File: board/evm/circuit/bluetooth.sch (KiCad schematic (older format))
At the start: 1 part

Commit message: add lots of ICs
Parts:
- removed U?: STM32F405VGTx, LQFP100, symbol STM32F405VGTx
- added U?: DA14580-QFN40, symbol DA14580-QFN40
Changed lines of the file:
@@
 EELAYER 25 0
 EELAYER END
-$Descr A2 23386 16535
+$Descr A4 11693 8268
 encoding utf-8
-Sheet 2 8
+Sheet 6 8
 Title ""
 Date ""
@@
 $EndDescr
 $Comp
-L STM32F405VGTx U?
-U 1 1 5753F449
-P 9650 6400
-F 0 "U?" H 5350 9225 50  0000 L BNN
-F 1 "STM32F405VGTx" H 13950 9225 50  0000 R BNN
-F 2 "LQFP100" H 13950 9175 50  0000 R TNN
-F 3 "" H 9650 6400 50  0000 C CNN
-	1    9650 6400
+L DA14580-QFN40 U?
+U 1 1 575491AD
+P 4450 2950
+F 0 "U?" H 4350 3000 60  0000 C CNN
+F 1 "DA14580-QFN40" H 4400 2850 60  0000 C CNN
+F 2 "" H 4350 3000 60  0000 C CNN
+F 3 "" H 4350 3000 60  0000 C CNN
+	1    4450 2950
 	1    0    0    -1
 $EndComp

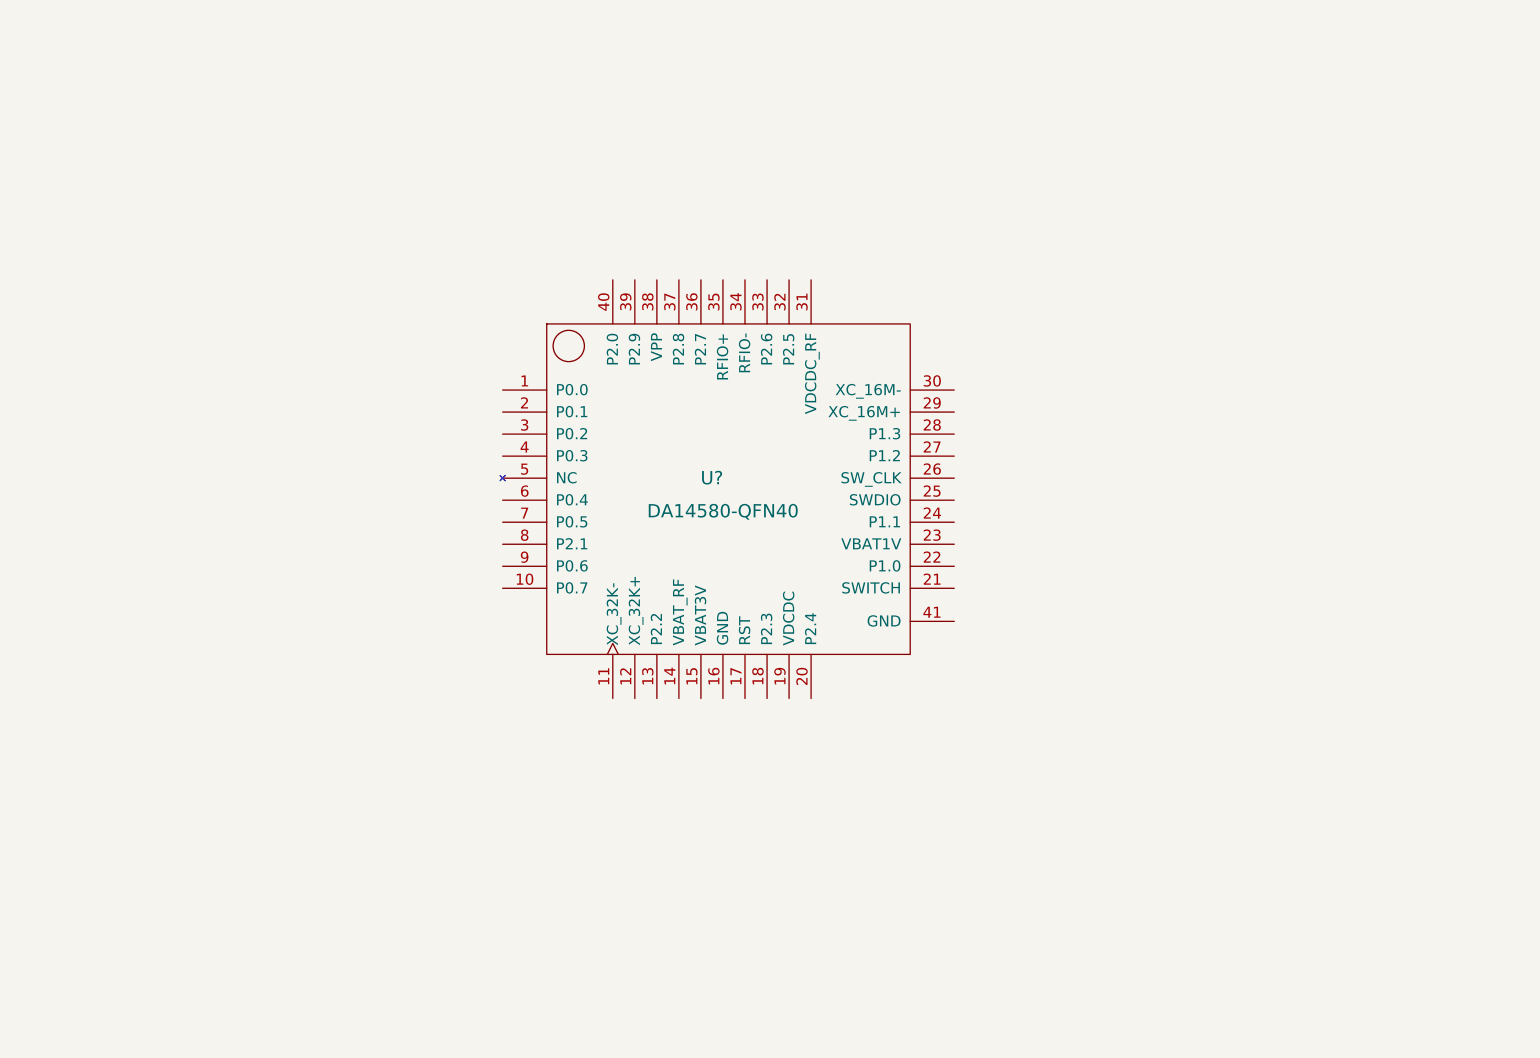
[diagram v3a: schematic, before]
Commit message: still working for sch
All done except for battery, which need more consideration on scheme of
QC2.0 (or QC3.0?), bidirectional charge.
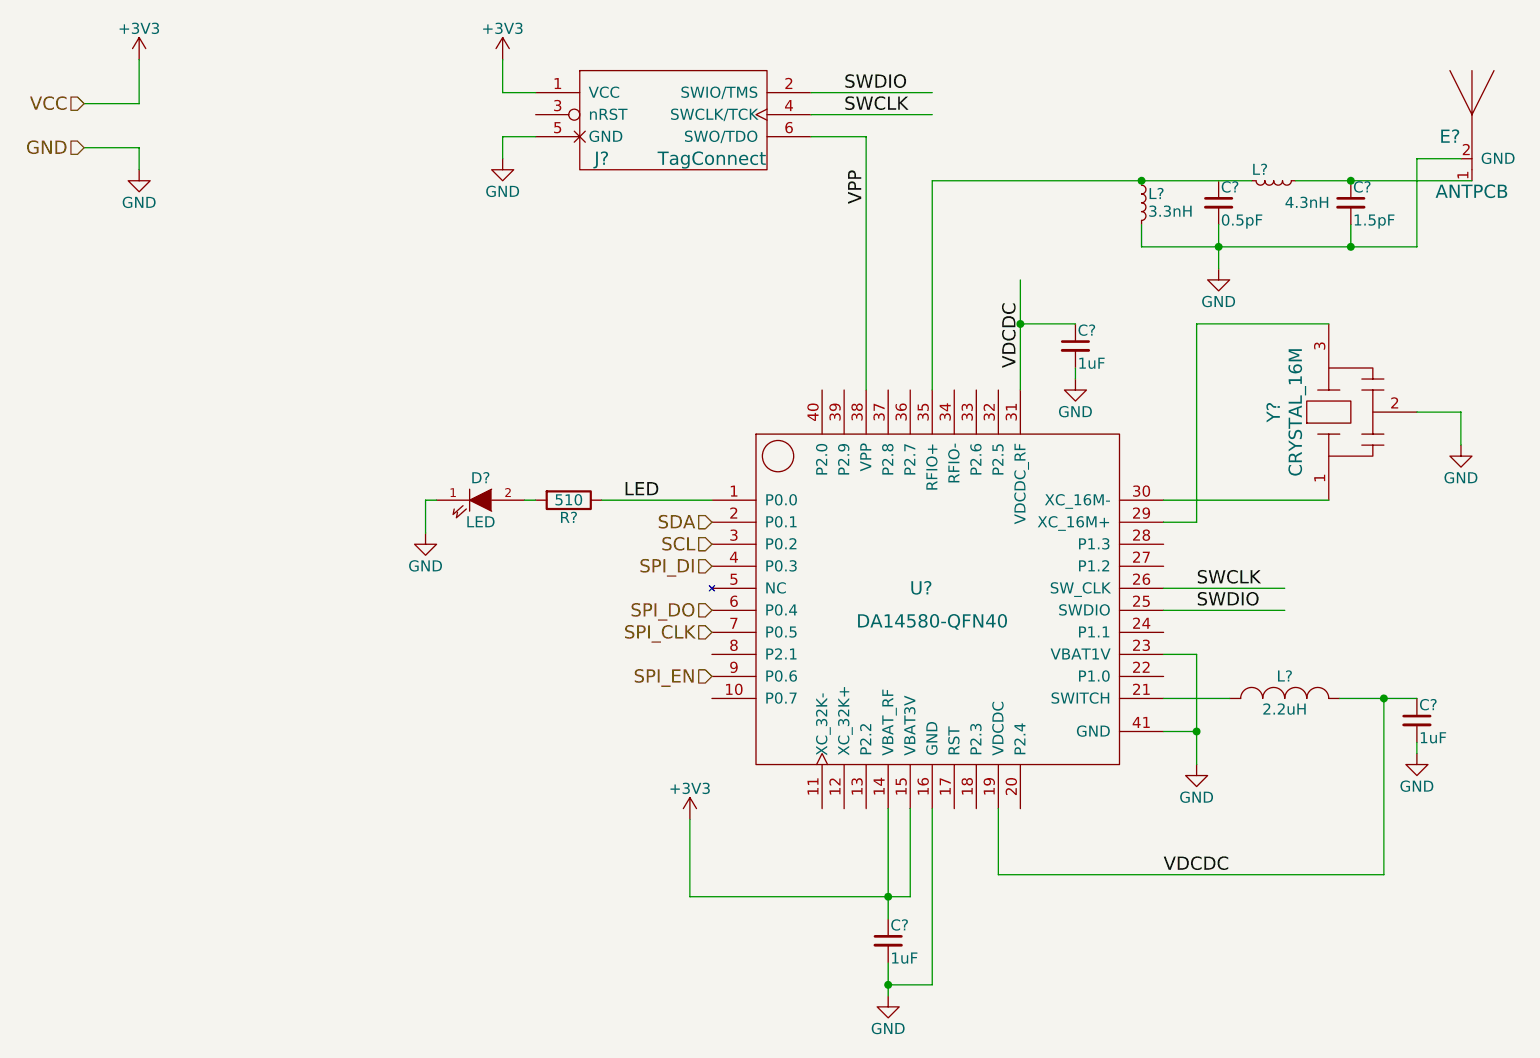
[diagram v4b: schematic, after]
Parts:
- added C? (x3): 1uF, symbol C_Small
- added C?: 0.5pF, symbol C_Small
- added C?: 1.5pF, symbol C_Small
- added D?: LED, symbol LED
- added E?: ANTPCB, symbol ANTPCB
- added J?: TagConnect, symbol TagConnect
- added L?: 2.2uH, symbol INDUCTOR_SMALL
- added L?: 3.3nH, symbol L_Small
- added L?: 4.3nH, symbol L_Small
- added R?: 510, symbol R
- added Y?: CRYSTAL_16M, symbol CRYSTAL_SMT
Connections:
- net labels added: +3V3, GND, LED, SCL, SDA, SPI_CLK, SPI_DI, SPI_DO, SPI_EN, SWCLK, SWDIO, VCC, VDCDC, VPP
- wire segments 0 -> 63
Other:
- moved on the sheet: U?

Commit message: working on qc3
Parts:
- gave numbers to parts that had none: 14
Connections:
- wire segments 63 -> 52
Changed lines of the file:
@@
 LIBS:contrib
 LIBS:valves
+LIBS:stm8
+LIBS:stm32
+LIBS:74xgxx
+LIBS:ac-dc
+LIBS:actel
 LIBS:Altera
-LIBS:my_kicad
+LIBS:analog_devices
+LIBS:battery_management
+LIBS:bbd
+LIBS:brooktre
+LIBS:cmos_ieee
+LIBS:dc-dc
+LIBS:diode
+LIBS:elec-unifil
+LIBS:ESD_Protection
+LIBS:ftdi
+LIBS:gennum
+LIBS:graphic
+LIBS:hc11
+LIBS:ir
+LIBS:Lattice
+LIBS:logo
+LIBS:maxim
+LIBS:microchip_dspic33dsc
+LIBS:microchip_pic10mcu
+LIBS:microchip_pic12mcu
+LIBS:microchip_pic16mcu
+LIBS:microchip_pic18mcu
+LIBS:microchip_pic32mcu
+LIBS:motor_drivers
+LIBS:msp430
+LIBS:nordicsemi
+LIBS:nxp_armmcu
+LIBS:onsemi
 LIBS:Oscillators
+LIBS:powerint
+LIBS:Power_Management
+LIBS:pspice
+LIBS:references
+LIBS:relays
+LIBS:rfcom
+LIBS:sensors
+LIBS:silabs
+LIBS:supertex
+LIBS:switches
+LIBS:transf
+LIBS:ttl_ieee
+LIBS:video
+LIBS:Worldsemi
+LIBS:Xicor
+LIBS:Zilog
 LIBS:oh-my-keyboard-cache
 EELAYER 25 0
@@
 $EndDescr
 $Comp
-L DA14580-QFN40 U?
+L DA14580-QFN40 U7
 U 1 1 575491AD
 P 5400 3450
-F 0 "U?" H 5300 3500 60  0000 C CNN
+F 0 "U7" H 5300 3500 60  0000 C CNN
 F 1 "DA14580-QFN40" H 5350 3350 60  0000 C CNN
 F 2 "" H 5300 3500 60  0000 C CNN
@@
 SCL
 $Comp
-L +3V3 #PWR?
+L +3V3 #PWR062
 U 1 1 57594899
 P 1750 1000
-F 0 "#PWR?" H 1750 850 50  0001 C CNN
+F 0 "#PWR062" H 1750 850 50  0001 C CNN
 F 1 "+3V3" H 1750 1140 50  0000 C CNN
 F 2 "" H 1750 1000 50  0000 C CNN
@@
 	1750 1200 1750 1000
 $Comp
-L GND #PWR?
+L GND #PWR063
 U 1 1 575948B2
 P 1750 1500
-F 0 "#PWR?" H 1750 1250 50  0001 C CNN
+F 0 "#PWR063" H 1750 1250 50  0001 C CNN
 F 1 "GND" H 1750 1350 50  0000 C CNN
 F 2 "" H 1750 1500 50  0000 C CNN
@@
 	1750 1400 1750 1500
 $Comp
-L +3V3 #PWR?
+L +3V3 #PWR064
 U 1 1 575948CE
 P 4250 4450
-F 0 "#PWR?" H 4250 4300 50  0001 C CNN
+F 0 "#PWR064" H 4250 4300 50  0001 C CNN
 F 1 "+3V3" H 4250 4590 50  0000 C CNN
 F 2 "" H 4250 4450 50  0000 C CNN
@@
 	4250 4450 4250 4800
 Wire Wire Line
-	4250 4800 5150 4800
-Wire Wire Line
-	5150 4800 5250 4800
-Wire Wire Line
-	5150 4400 5150 4800
-Wire Wire Line
-	5150 4800 5150 4900
+	4250 4800 5250 4800
+Wire Wire Line
+	5150 4400 5150 4900
 Wire Wire Line
 	5250 4800 5250 4400
 Connection ~ 5150 4800
 $Comp
-L C_Small C?
+L C_Small C10
 U 1 1 57594902
 P 5150 5000
-F 0 "C?" H 5160 5070 50  0000 L CNN
+F 0 "C10" H 5160 5070 50  0000 L CNN
 F 1 "1uF" H 5160 4920 50  0000 L CNN
 F 2 "" H 5150 5000 50  0000 C CNN
@@
 $EndComp
 $Comp
-L GND #PWR?
+L GND #PWR065
 U 1 1 57594985
 P 5150 5250
-F 0 "#PWR?" H 5150 5000 50  0001 C CNN
+F 0 "#PWR065" H 5150 5000 50  0001 C CNN
 F 1 "GND" H 5150 5100 50  0000 C CNN
 F 2 "" H 5150 5250 50  0000 C CNN
@@
 $EndComp
 Wire Wire Line
-	5150 5100 5150 5200
-Wire Wire Line
-	5150 5200 5150 5250
+	5150 5100 5150 5250
 Wire Wire Line
 	5350 4400 5350 5200
@@
 Connection ~ 5150 5200
 $Comp
-L GND #PWR?
+L GND #PWR066
 U 1 1 575949DB
 P 6550 4200
-F 0 "#PWR?" H 6550 3950 50  0001 C CNN
+F 0 "#PWR066" H 6550 3950 50  0001 C CNN
 F 1 "GND" H 6550 4050 50  0000 C CNN
 F 2 "" H 6550 4200 50  0000 C CNN
@@
 	6400 4050 6550 4050
 Wire Wire Line
-	6550 3700 6550 4050
-Wire Wire Line
-	6550 4050 6550 4200
-$Comp
-L INDUCTOR_SMALL L?
+	6550 3700 6550 4200
+$Comp
+L INDUCTOR_SMALL L6
 U 1 1 57594A20
 P 6950 3900
-F 0 "L?" H 6950 4000 50  0000 C CNN
+F 0 "L6" H 6950 4000 50  0000 C CNN
 F 1 "2.2uH" H 6950 3850 50  0000 C CNN
 F 2 "" H 6950 3900 50  0000 C CNN
@@
 	6400 3900 6700 3900
 Wire Wire Line
-	7200 3900 7400 3900
-Wire Wire Line
-	7400 3900 7550 3900
+	7200 3900 7550 3900
 Wire Wire Line
 	7400 3900 7400 4700
@@
 VDCDC
 Wire Wire Line
-	5750 2000 5750 2200
-Wire Wire Line
-	5750 2200 5750 2500
+	5750 2000 5750 2500
 Text Label 5750 2400 1    60   ~ 0
 VDCDC
 $Comp
-L C_Small C?
+L C_Small C11
 U 1 1 57594AAC
 P 6000 2300
-F 0 "C?" H 6010 2370 50  0000 L CNN
+F 0 "C11" H 6010 2370 50  0000 L CNN
 F 1 "1uF" H 6010 2220 50  0000 L CNN
 F 2 "" H 6000 2300 50  0000 C CNN
@@
 Connection ~ 5750 2200
 $Comp
-L GND #PWR?
+L GND #PWR067
 U 1 1 57594B38
 P 6000 2450
-F 0 "#PWR?" H 6000 2200 50  0001 C CNN
+F 0 "#PWR067" H 6000 2200 50  0001 C CNN
 F 1 "GND" H 6000 2300 50  0000 C CNN
 F 2 "" H 6000 2450 50  0000 C CNN
@@
 Connection ~ 6550 4050
 $Comp
-L CRYSTAL_SMT Y?
+L CRYSTAL_SMT Y2
 U 1 1 57594EC4
 P 7200 2600
-F 0 "Y?" H 7200 2900 60  0000 C CNN
+F 0 "Y2" H 7200 2900 60  0000 C CNN
 F 1 "CRYSTAL_16M" H 7200 2800 60  0000 C CNN
 F 2 "" H 7200 2600 60  0000 C CNN
@@
 	6550 3100 6400 3100
 $Comp
-L GND #PWR?
+L GND #PWR068
 U 1 1 57594FC8
 P 7750 2750
-F 0 "#PWR?" H 7750 2500 50  0001 C CNN
+F 0 "#PWR068" H 7750 2500 50  0001 C CNN
 F 1 "GND" H 7750 2600 50  0000 C CNN
 F 2 "" H 7750 2750 50  0000 C CNN
@@
 	7750 2600 7750 2750
 $Comp
-L TagConnect J?
+L TagConnect J2
 U 1 1 57595027
 P 4150 1300
-F 0 "J?" H 3850 1150 60  0000 C CNN
+F 0 "J2" H 3850 1150 60  0000 C CNN
 F 1 "TagConnect" H 4350 1150 60  0000 C CNN
 F 2 "" H 4000 1350 60  0000 C CNN
@@
 $EndComp
 $Comp
-L +3V3 #PWR?
+L +3V3 #PWR069
 U 1 1 5759512A
 P 3400 1000
-F 0 "#PWR?" H 3400 850 50  0001 C CNN
+F 0 "#PWR069" H 3400 850 50  0001 C CNN
 F 1 "+3V3" H 3400 1140 50  0000 C CNN
 F 2 "" H 3400 1000 50  0000 C CNN
@@
 	3400 1150 3550 1150
 $Comp
-L GND #PWR?
+L GND #PWR070
 U 1 1 5759517F
 P 3400 1450
-F 0 "#PWR?" H 3400 1200 50  0001 C CNN
+F 0 "#PWR070" H 3400 1200 50  0001 C CNN
 F 1 "GND" H 3400 1300 50  0000 C CNN
 F 2 "" H 3400 1450 50  0000 C CNN
@@
 SWCLK
 $Comp
-L C_Small C?
+L C_Small C14
 U 1 1 575956A9
 P 7550 4000
-F 0 "C?" H 7560 4070 50  0000 L CNN
+F 0 "C14" H 7560 4070 50  0000 L CNN
 F 1 "1uF" H 7560 3920 50  0000 L CNN
 F 2 "" H 7550 4000 50  0000 C CNN
@@
 $EndComp
 $Comp
-L GND #PWR?
+L GND #PWR071
 U 1 1 57595724
 P 7550 4150
-F 0 "#PWR?" H 7550 3900 50  0001 C CNN
+F 0 "#PWR071" H 7550 3900 50  0001 C CNN
 F 1 "GND" H 7550 4000 50  0000 C CNN
 F 2 "" H 7550 4150 50  0000 C CNN
@@
 Connection ~ 7400 3900
 $Comp
-L L_Small L?
+L L_Small L4
 U 1 1 57595AEB
 P 6300 1650
-F 0 "L?" H 6330 1690 50  0000 L CNN
+F 0 "L4" H 6330 1690 50  0000 L CNN
 F 1 "3.3nH" H 6330 1610 50  0000 L CNN
 F 2 "" H 6300 1650 50  0000 C CNN
@@
 $EndComp
 $Comp
-L L_Small L?
+L L_Small L5
 U 1 1 57595B48
 P 6900 1550
-F 0 "L?" V 6850 1450 50  0000 L CNN
+F 0 "L5" V 6850 1450 50  0000 L CNN
 F 1 "4.3nH" V 7000 1600 50  0000 L CNN
 F 2 "" H 6900 1550 50  0000 C CNN
@@
 	5350 2500 5350 1550
 Wire Wire Line
-	5350 1550 6300 1550
-Wire Wire Line
-	6300 1550 6800 1550
+	5350 1550 6800 1550
 Connection ~ 6300 1550
 $Comp
-L C_Small C?
+L C_Small C12
 U 1 1 57595F02
 P 6650 1650
-F 0 "C?" H 6660 1720 50  0000 L CNN
+F 0 "C12" H 6660 1720 50  0000 L CNN
 F 1 "0.5pF" H 6660 1570 50  0000 L CNN
 F 2 "" H 6650 1650 50  0000 C CNN
@@
 	6300 1750 6300 1850
 Wire Wire Line
-	6300 1850 6650 1850
-Wire Wire Line
-	6650 1850 7250 1850
-Wire Wire Line
-	7250 1850 7550 1850
-Wire Wire Line
-	6650 1750 6650 1850
-Wire Wire Line
-	6650 1850 6650 1950
-$Comp
-L GND #PWR?
+	6300 1850 7550 1850
+Wire Wire Line
+	6650 1750 6650 1950
+$Comp
+L GND #PWR072
 U 1 1 57595FB6
 P 6650 1950
-F 0 "#PWR?" H 6650 1700 50  0001 C CNN
+F 0 "#PWR072" H 6650 1700 50  0001 C CNN
 F 1 "GND" H 6650 1800 50  0000 C CNN
 F 2 "" H 6650 1950 50  0000 C CNN
@@
 $EndComp
 $Comp
-L C_Small C?
+L C_Small C13
 U 1 1 57596029
 P 7250 1650
-F 0 "C?" H 7260 1720 50  0000 L CNN
+F 0 "C13" H 7260 1720 50  0000 L CNN
 F 1 "1.5pF" H 7260 1570 50  0000 L CNN
 F 2 "" H 7250 1650 50  0000 C CNN
@@
 $EndComp
 Wire Wire Line
-	7000 1550 7250 1550
-Wire Wire Line
-	7250 1550 7800 1550
+	7000 1550 7800 1550
 Wire Wire Line
 	7250 1850 7250 1750
 Connection ~ 6650 1850
 $Comp
-L ANTPCB E?
+L ANTPCB E2
 U 1 1 57596217
 P 7800 1500
-F 0 "E?" H 7700 1650 60  0000 C CNN
+F 0 "E2" H 7700 1650 60  0000 C CNN
 F 1 "ANTPCB" H 7800 1400 60  0000 C CNN
 F 2 "" H 7800 1500 60  0000 C CNN
@@
 Connection ~ 7250 1850
 $Comp
-L LED D?
+L LED D9
 U 1 1 57596385
 P 3300 3000
-F 0 "D?" H 3300 3100 50  0000 C CNN
+F 0 "D9" H 3300 3100 50  0000 C CNN
 F 1 "LED" H 3300 2900 50  0000 C CNN
 F 2 "" H 3300 3000 50  0000 C CNN
@@
 	3850 3000 4350 3000
 $Comp
-L R R?
+L R R7
 U 1 1 5759657F
 P 3700 3000
-F 0 "R?" V 3780 3000 50  0000 C CNN
+F 0 "R7" V 3780 3000 50  0000 C CNN
 F 1 "510" V 3700 3000 50  0000 C CNN
 F 2 "" V 3630 3000 50  0000 C CNN
@@
 	3550 3000 3500 3000
 $Comp
-L GND #PWR?
+L GND #PWR073
 U 1 1 5759667C
 P 3050 3150
-F 0 "#PWR?" H 3050 2900 50  0001 C CNN
+F 0 "#PWR073" H 3050 2900 50  0001 C CNN
 F 1 "GND" H 3050 3000 50  0000 C CNN
 F 2 "" H 3050 3150 50  0000 C CNN
